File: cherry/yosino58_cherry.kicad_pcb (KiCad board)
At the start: 2 copper layers, 156.8 x 135 mm, 121 parts, among them J0 LED, J1 TRRS, J2 OLED, J3 OLED, J4 OLED, J5 OLED, J6 OLED, P1 i2c_pin, P2 i2c_pin, SW1 SW_PUSH, SW10 SW_PUSH, SW11 SW_PUSH, SW12 SW_PUSH, SW13 SW_PUSH, SW14 SW_PUSH, SW15 SW_PUSH, SW16 SW_PUSH, SW17 SW_PUSH, SW18 SW_PUSH, SW19 SW_PUSH, SW2 SW_PUSH, SW20 SW_PUSH, SW21 SW_PUSH, SW22 SW_PUSH, SW23 SW_PUSH, SW24 SW_PUSH, SW25 SW_PUSH, SW26 SW_PUSH, SW27 SW_PUSH, SW28 SW_PUSH, SW29 SW_PUSH, SW3 SW_PUSH, SW4 SW_PUSH, SW5 SW_PUSH, SW6 SW_PUSH, SW7 SW_PUSH, SW8 SW_PUSH, SW9 SW_PUSH, U1 ProMicro, U2 ProMicro

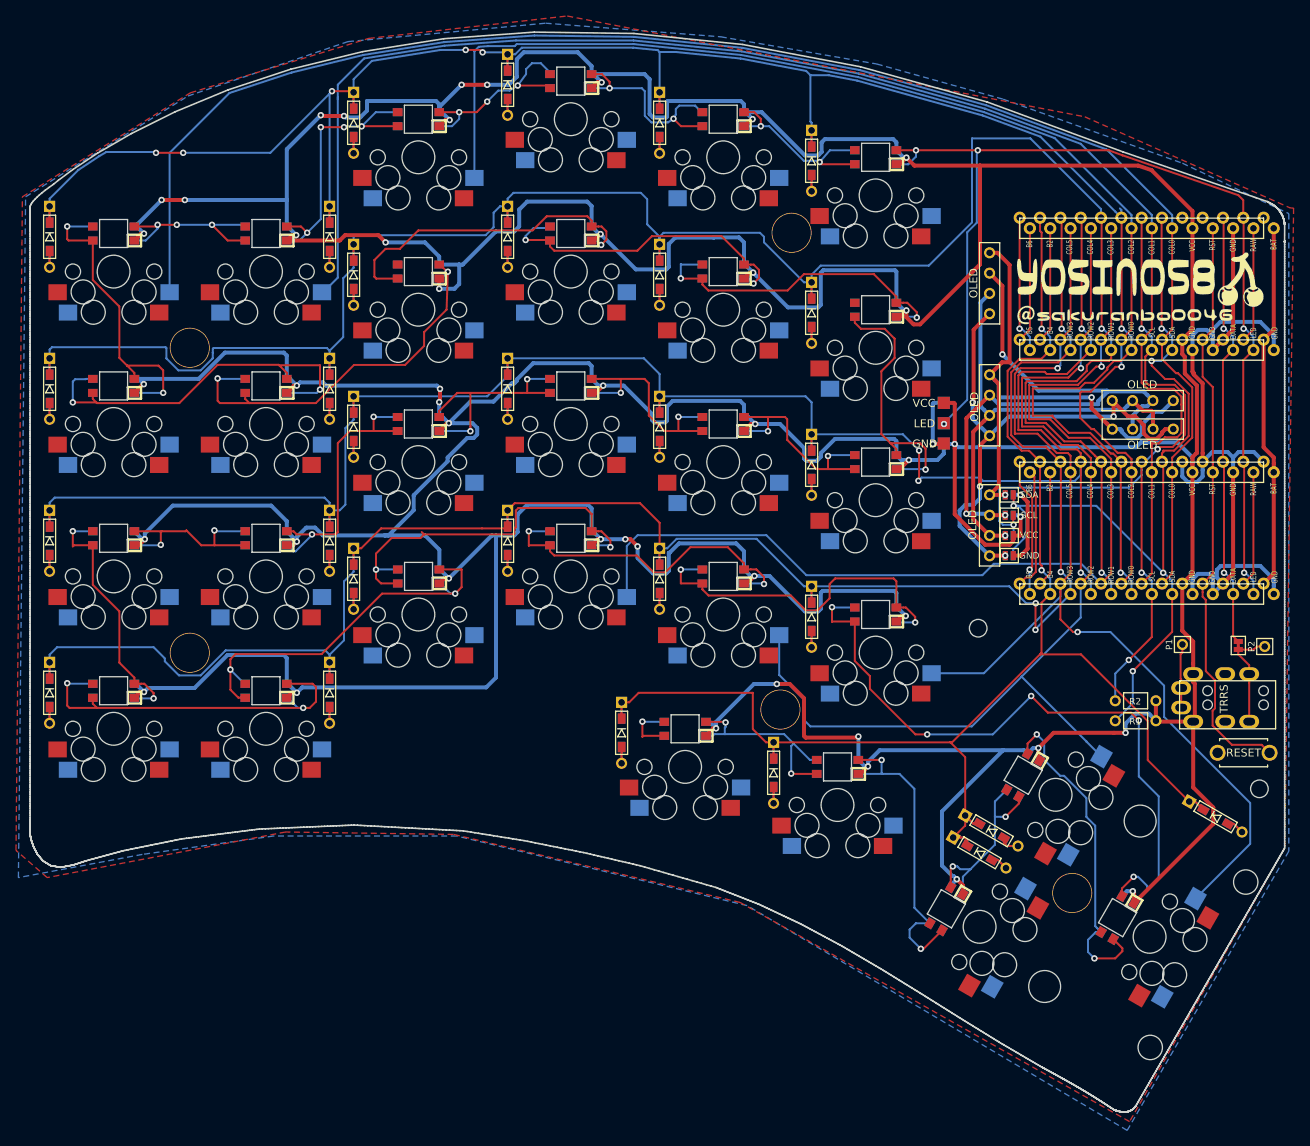
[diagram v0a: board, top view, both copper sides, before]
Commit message: ソケット版追加
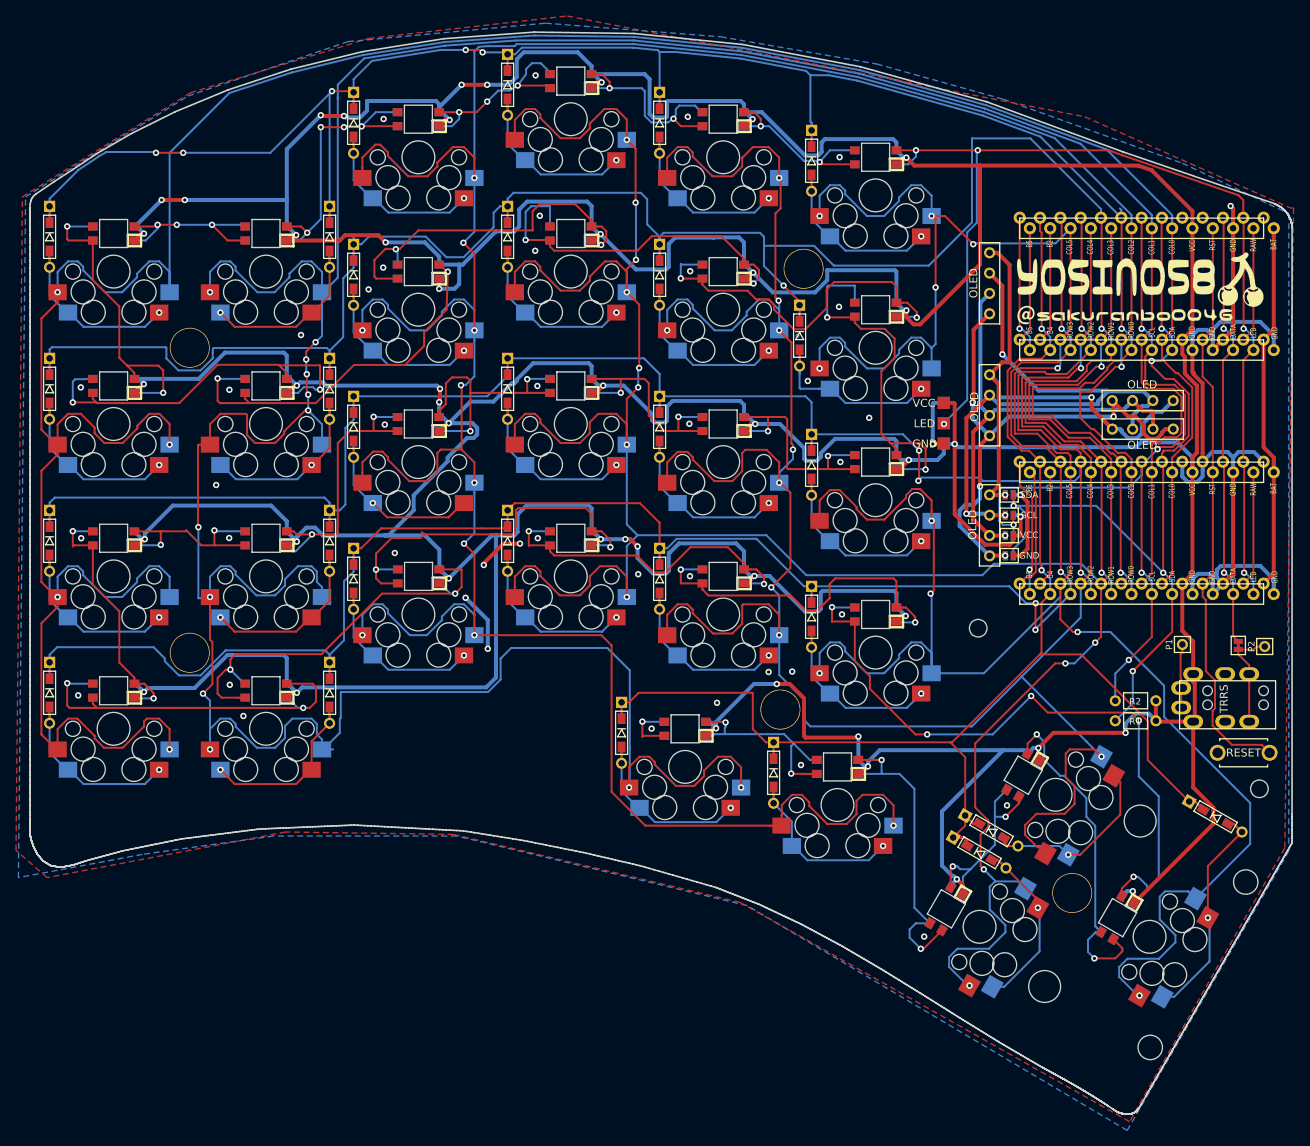
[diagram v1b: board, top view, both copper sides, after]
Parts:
- removed the G*** at (125.3, 81.1)
- added G***: LOGO, yosino58_cherry:sakura_rev, F.Cu at (123.7, 90.5)
- L1, L10, L11, L12, L13, L14, L15, L16, L17, L18, L19, L2, L20, L21, L22, L23, L24, L25, L26, L27, L28, L29, L3, L4, L5, L6, L7, L8, L9: footprint yosino58_cherry:SK6812MINI_padin_rev -> yosino58_cherry:SK6812MINI_rev
- moved Ref** 4.74 mm to (136.8, 52.0)
- moved D12 3.22 mm to (136.2, 60.4)
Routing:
- net col1: track 189.8 -> 434.2 mm, vias 0 -> 12
- net col2: track 157.6 -> 394.1 mm, vias 1 -> 11
- net col3: track 130.5 -> 350.4 mm, vias 1 -> 13
- net col4: track 129.2 -> 309.5 mm, vias 1 -> 10
- net col5: track 132.4 -> 308.5 mm, vias 2 -> 11
- net col0: track 201.9 -> 359.7 mm, vias 0 -> 4
- net Net-(D29-Pad2): track 4.37 -> 30.1 mm, vias 0 -> 1
- net Net-(D12-Pad2): track 4.07 -> 25.9 mm, vias 0 -> 1
- net Net-(D28-Pad2): track 5.13 -> 25.6 mm, vias 0 -> 1
- net Net-(D27-Pad2): track 4.37 -> 24.3 mm, vias 0 -> 1
- net Net-(D21-Pad2): track 4.07 -> 23.8 mm, vias 0 -> 1
- net Net-(D19-Pad2): track 4.07 -> 23.8 mm, vias 0 -> 1
- net Net-(D24-Pad2): track 4.07 -> 23.8 mm, vias 0 -> 1
- net Net-(D15-Pad2): track 4.07 -> 23.8 mm, vias 0 -> 1
- net Net-(D13-Pad2): track 4.07 -> 23.7 mm, vias 0 -> 1
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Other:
- board size 156.8 x 135 mm -> 157.8 x 135.3 mm
